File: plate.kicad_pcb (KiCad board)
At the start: 2 copper layers, 95 x 95 mm, 4 parts, among them M8 MountingHole_8.4mm_M8

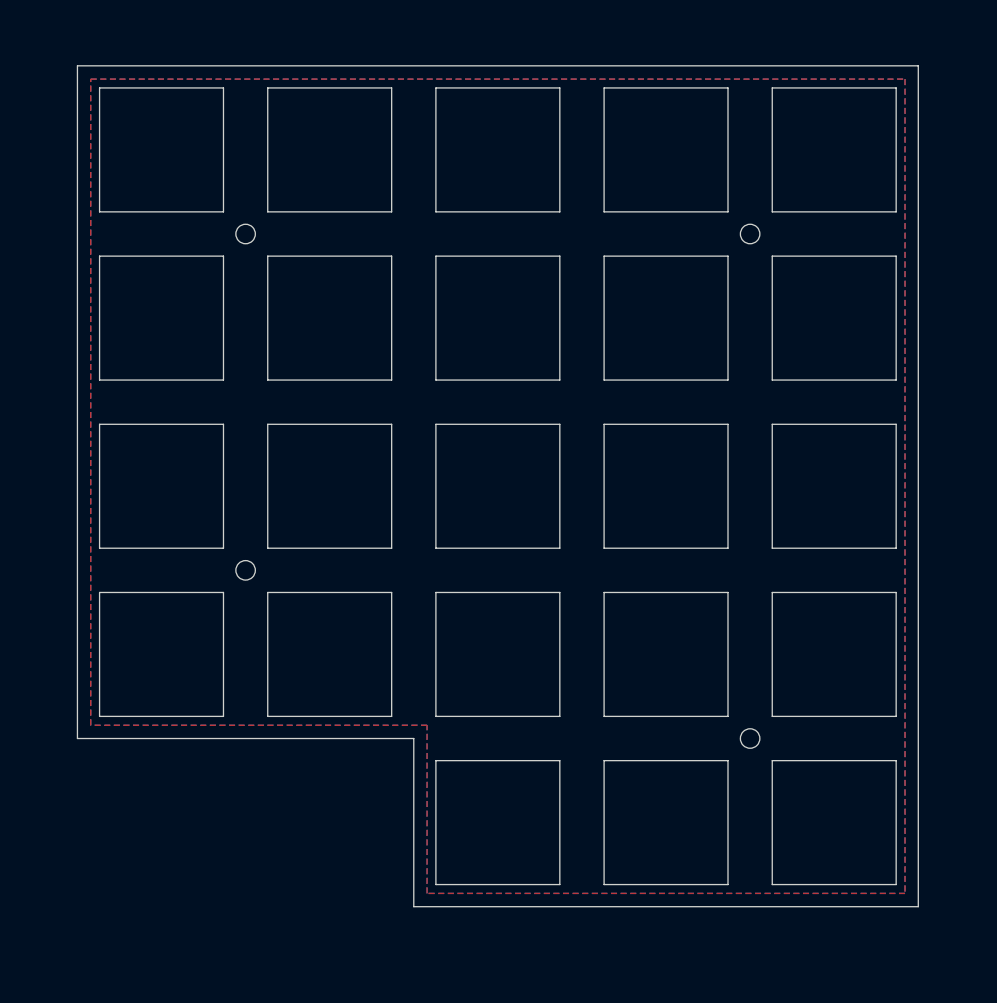
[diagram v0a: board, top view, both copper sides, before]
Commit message: Change plate outer borders to match jlcpcb specs (4mm, was 2.54mm), round corners, force Cu GND zones with 1mm^2 pads
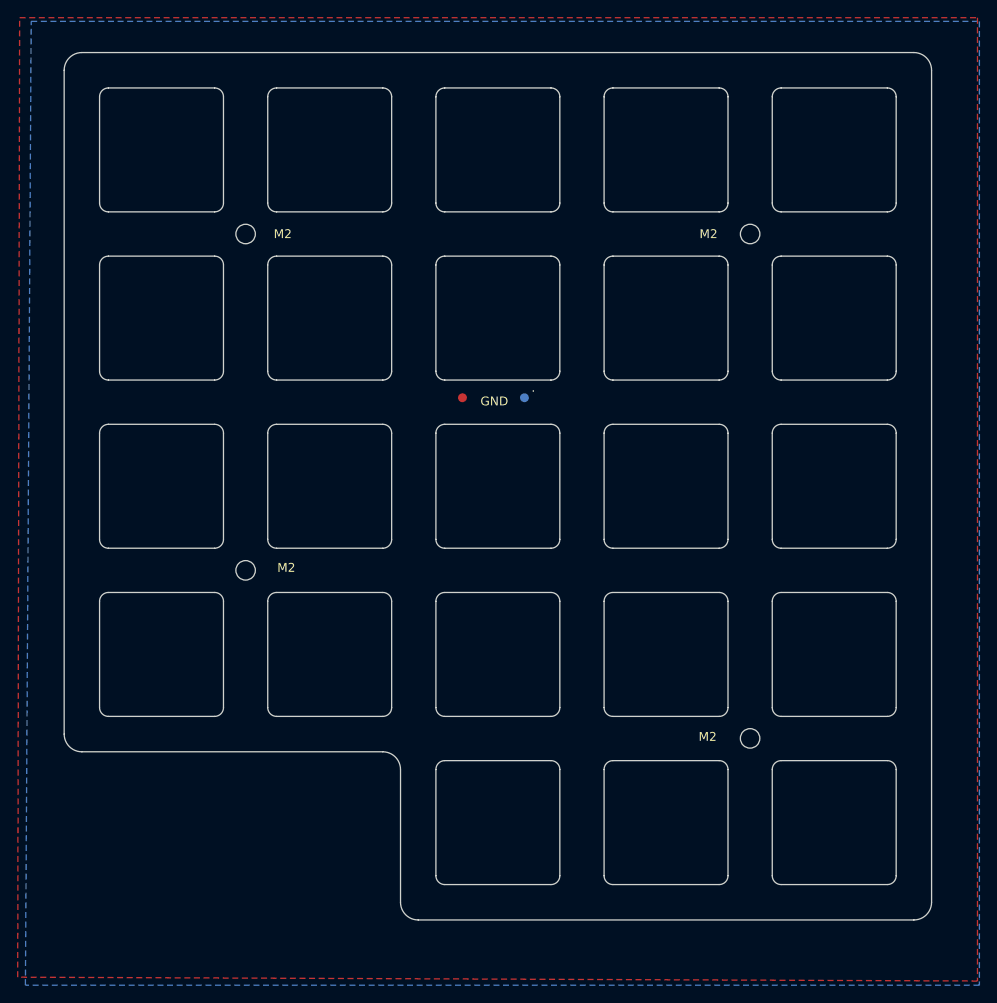
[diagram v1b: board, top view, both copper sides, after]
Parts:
- added .: ., TestPoint:TestPoint_Pad_1.0x1.0mm, F.Cu at (131.0, 82.3)
- added .: ., TestPoint:TestPoint_Pad_1.0x1.0mm, F.Cu at (123.3, 82.4)
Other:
- board size 95 x 95 mm -> 98 x 98 mm
- board text added: "For Science"
- board text added: "GND"
- board text added: "M2"
